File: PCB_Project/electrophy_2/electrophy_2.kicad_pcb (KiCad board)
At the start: 4 copper layers, 35 x 35 mm, 46 parts, among them IC1 ESP32-C3FN4, J1 USB_C_Receptacle_USB2.0_14P, J3 Conn_01x04, SW2 SW_Push, U1 LSM6DSV320XTR, U2 BQ21040DBV, U3 TPS27081ADDCR, U4 USBLC6-2SC6, U5 MIC5504-3.3YM5, Y1 40MHZ 15pf, Y2 32 KHz

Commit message: PCB draft
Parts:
- removed G***: LOGO, ESP32 IMU:Electrophy logo
- J3: footprint Connector_FFC-FPC:Amphenol_F32R-1A7x1-11004_1x04-1MP_P0.5mm_Horizontal -> pogo_pads_4:pogo_pads_4; moved to B.Cu
- moved R10 79.2 mm to (159.5, 112.0), turned to 90 degrees
- moved CH 76.2 mm to (161.2, 111.2), turned to 45 degrees
- moved R11 75.0 mm to (156.4, 110.2)
- moved R12 66.8 mm to (150.6, 103.2)
- moved R13 64.0 mm to (148.3, 103.2)
- moved R14 54.5 mm to (137.3, 104.2), turned to 45 degrees
- moved R15 51.7 mm to (136.4, 103.4), turned to -135 degrees
- moved R9 50.7 mm to (153.6, 113.1), turned to -90 degrees
- moved C1 34.1 mm to (147.8, 112.9), turned to -135 degrees
- moved C10 33.1 mm to (152.8, 101.4), turned to -90 degrees
- moved C12 26.3 mm to (141.1, 101.4)
- moved J3 23.0 mm to (159.6, 90.5), turned to 135 degrees
- moved R3 18.9 mm to (153.1, 110.1), turned to 90 degrees
- moved C3 18.6 mm to (146.2, 112.8), turned to -135 degrees
- moved C2 14.8 mm to (151.4, 107.0), turned to 90 degrees
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- renumbered STA2 to CH, SW2 to ON, STA1 to S1
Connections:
- BAT1 pad 1: BAT_V -> Net-(BAT1-Pin_1)
- C2 pad 1: Net-(U5-VIN) -> BAT_V
- J3 pad 3: SDA -> SCL
- J3 pad 4: SCL -> SDA
- ON pad 1: BAT_V -> Net-(BAT1-Pin_1)
- R11 pad 1: BAT_V -> Net-(BAT1-Pin_1)
- R13 pad 1: BAT_V -> Net-(BAT1-Pin_1)
- R3 pad 1: Net-(U5-VIN) -> BAT_V
- U2 pad 2: BAT_V -> Net-(BAT1-Pin_1)
- U3 pad 2: Net-(U5-VIN) -> BAT_V
- U3 pad 3: Net-(U5-VIN) -> BAT_V
- U3 pad 4: BAT_V -> Net-(BAT1-Pin_1)
- U5 pad 1: Net-(U5-VIN) -> BAT_V
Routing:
- net GND: track 23.5 -> 83.1 mm, vias 32 -> 41
- net POWER_HOLD: track 0.00 -> 42.4 mm, vias 0 -> 2
- net SCL: track 0.75 -> 39.1 mm, vias 0 -> 3
- net Net-(BAT1-Pin_1): track 0.00 -> 38.0 mm, vias 0 -> 2
- net +3.3V: track 3.07 -> 34.3 mm, vias 1 -> 10
- net SDA: track 0.00 -> 27.9 mm, vias 0 -> 1
- net CS: track 0.00 -> 27.6 mm, vias 0 -> 2
- net VBUS: track 6.68 -> 32.2 mm
- net BAT_V: track 0.00 -> 25.2 mm, vias 0 -> 2
- net SCLK: track 0.00 -> 22.6 mm, vias 0 -> 2
- net MOSI: track 0.00 -> 16.5 mm, vias 0 -> 2
- net BAT_MON: track 0.51 -> 16.3 mm
- net MISO: track 0.00 -> 15.5 mm, vias 0 -> 2
- net INT1: track 0.00 -> 14.5 mm, vias 0 -> 2
- net Net-(IC1-GPIO8): track 0.00 -> 8.82 mm, vias 0 -> 2
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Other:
- rule solder_mask_min_width: 0.125 -> 0.1524
- board text added: "3.3v"
- board text added: "ELECTROPHY 2.0"
- board text added: "GND"
- board text added: "SCL"
- board text added: "SDA"
- board text added: "V1"
- board text removed: "BATTERY"
- board text removed: "PWR"
- board text removed: "S"
- board text removed: "V2"

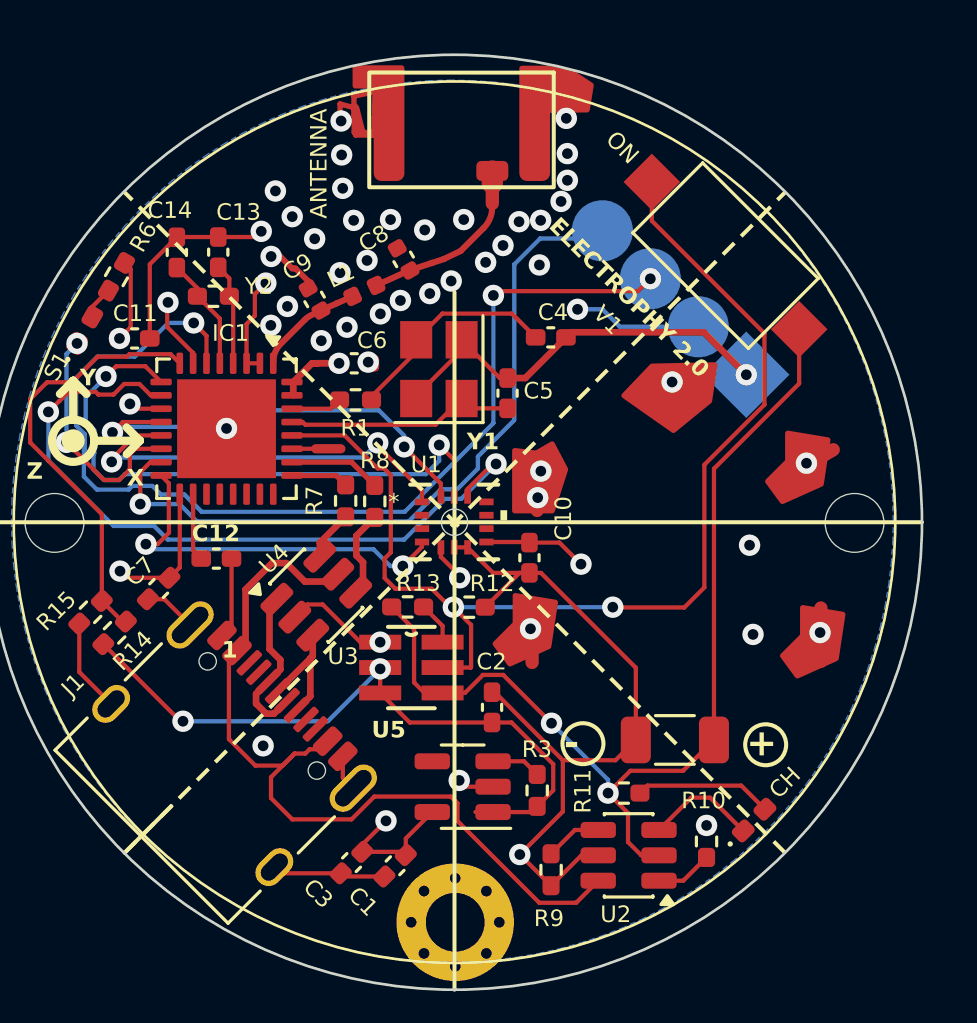
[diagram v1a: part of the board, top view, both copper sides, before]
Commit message: added CC1 and CC2 resistors
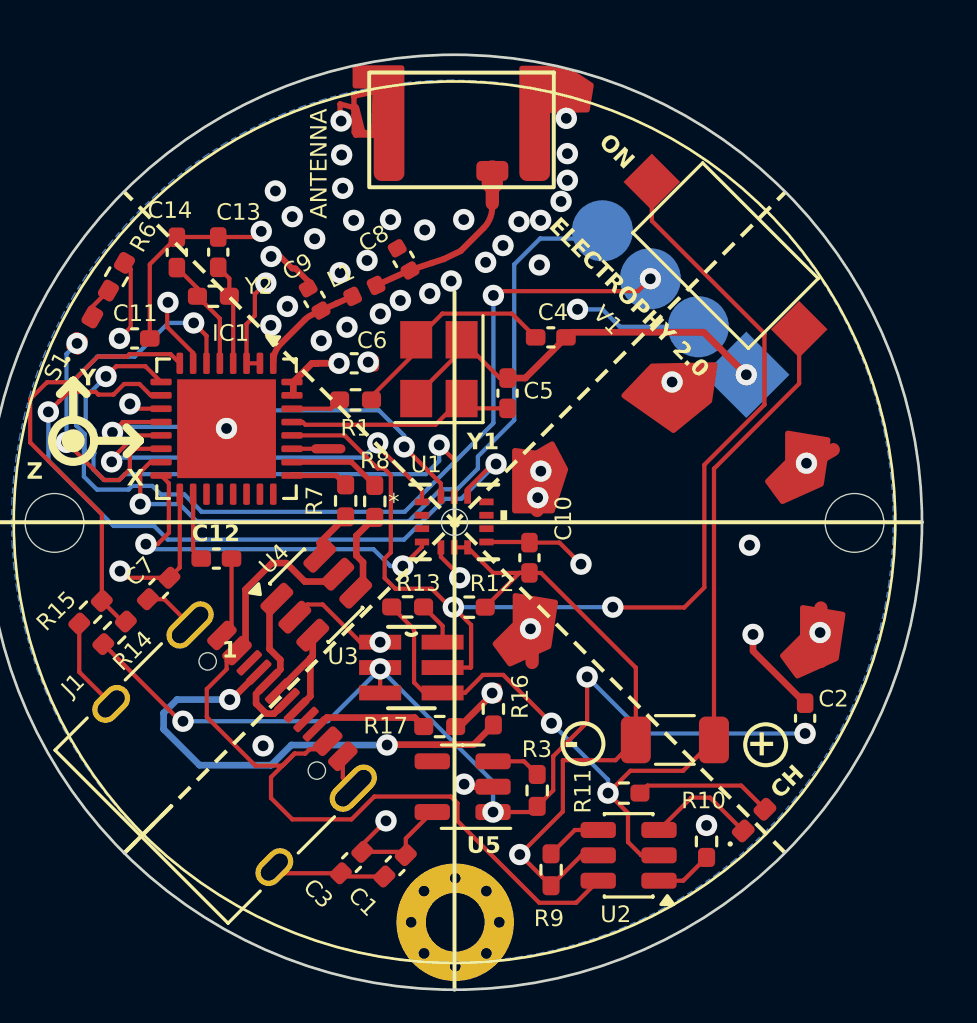
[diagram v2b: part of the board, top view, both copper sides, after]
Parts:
- added R16: 5.1k, Resistor_SMD:R_0402_1005Metric_Pad0.72x0.64mm_HandSolder, F.Cu at (151.5, 107.0)
- added R17: 5.1k, Resistor_SMD:R_0402_1005Metric_Pad0.72x0.64mm_HandSolder, F.Cu at (149.5, 107.7)
- moved C2 11.7 mm to (163.2, 107.4)
- renumbered CH to CH1, ON to ON1
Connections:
- J1 pad A5: unconnected-(J1-CC1-PadA5) -> Net-(J1-CC1)
- J1 pad B5: unconnected-(J1-CC2-PadB5) -> Net-(J1-CC2)
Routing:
- net Net-(J1-CC1): track 0.00 -> 18.3 mm, vias 0 -> 2
- net BAT_V: track 25.2 -> 36.9 mm, vias 2 -> 5
- net Net-(J1-CC2): track 0.00 -> 4.37 mm
- net GND: track 83.1 -> 84.5 mm, vias 41 -> 42
- net VBUS: track 32.2 -> 32.9 mm
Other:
- board text added: "CH"
- board text added: "ON"

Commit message: order placed for ElectroPhy 2.0 V1 PCB
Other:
- rule pad_to_mask_clearance: 0.08 -> 0
- board text removed: "Notes: OLED display pin pads under the PCB"
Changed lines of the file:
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@@
 			(dielectric_constraints yes)
 		)
-		(pad_to_mask_clearance 0.08)
-		(solder_mask_min_width 0.1524)
+		(pad_to_mask_clearance 0)
 		(allow_soldermask_bridges_in_footprints no)
 		(tenting
@@
 		(tags "resistor handsolder")
 		(property "Reference" "R6"
-			(at 1.795378 0.129686 60)
+			(at 0.441077 1.003968 60)
 			(layer "F.SilkS")
 			(effects
@@
 		(tags "capacitor handsolder")
 		(property "Reference" "C12"
-			(at -0.02 -0.94 0)
+			(at -0.09 -0.79 0)
 			(layer "F.SilkS")
 			(effects
@@
 		(tags "resistor handsolder")
 		(property "Reference" "R7"
-			(at 0 -1.17 90)
+			(at -0.21 -1.06 180)
 			(layer "F.SilkS")
 			(effects
@@
 		(tags "capacitor handsolder")
 		(property "Reference" "C10"
-			(at -1.47 -1.27 90)
+			(at 0.01 -0.93 90)
 			(layer "F.SilkS")
 			(effects
@@
 		(tags "capacitor handsolder")
 		(property "Reference" "C11"
-			(at 0.02 -0.94 0)
+			(at 0.57 -0.91 0)
 			(layer "F.SilkS")
 			(effects
@@
 		(tags "capacitor handsolder")
 		(property "Reference" "C14"
-			(at 1.58 -0.26 180)
+			(at 1.41 0.03 180)
 			(layer "F.SilkS")
 			(effects
@@
 		(tags "TPS27081ADDCR ")
 		(property "Reference" "U3"
-			(at -2.56 -0.42 0)
+			(at 2.77 -0.92 0)
 			(unlocked yes)
 			(layer "F.SilkS")
@@
 		(tags "QFN NoLead")
 		(property "Reference" "IC1"
-			(at -3.58 -0.15 0)
+			(at -3.62 -0.63 0)
 			(layer "F.SilkS")
 			(effects
@@
 		(tags "capacitor handsolder")
 		(property "Reference" "C6"
-			(at 0.67 -0.86 0)
+			(at 0.33 -0.83 0)
 			(layer "F.SilkS")
 			(effects
@@
 			(net "unconnected-(U1-SDX-Pad2)")
 			(pinfunction "SDX_2")
-			(pintype "unspecified")
+			(pintype "unspecified+no_connect")
 		)
 		(pad "3" smd rect
@@
 			(net "unconnected-(U1-SCX-Pad3)")
 			(pinfunction "SCX_3")
-			(pintype "unspecified")
+			(pintype "unspecified+no_connect")
 		)
 		(pad "4" smd rect
@@
 			(net "unconnected-(U1-INT2-Pad9)")
 			(pinfunction "INT2_9")
-			(pintype "unspecified")
+			(pintype "unspecified+no_connect")
 		)
 		(pad "10" smd rect
@@
 			(net "unconnected-(U1-OCS_AUX-Pad10)")
 			(pinfunction "OCS_AUX_10")
-			(pintype "unspecified")
+			(pintype "unspecified+no_connect")
 		)
 		(pad "11" smd rect
@@
 			(net "unconnected-(U1-SDO_AUX-Pad11)")
 			(pinfunction "SDO_AUX_11")
-			(pintype "unspecified")
+			(pintype "unspecified+no_connect")
 		)
 		(pad "12" smd rect
@@
 		(tags "LED handsolder")
 		(property "Reference" "S1"
-			(at -1.684134 -0.217006 60)
+			(at -1.671455 -0.155045 60)
 			(layer "F.SilkS")
 			(effects
@@
 		)
 	)
-	(gr_text "Notes:\nOLED display pin pads under the PCB"
-		(at 183.82 73.64 0)
-		(layer "Cmts.User")
-		(effects
-			(font
-				(size 0.62 0.62)
-				(thickness 0.15)
-				(bold yes)
-			)
-			(justify left bottom)
-		)
-	)
 	(dimension
 		(type aligned)
@@
 	)
 	(segment
+		(start 136.46625 91.98245)
+		(end 137.07125 91.37745)
+		(width 0.16)
+		(layer "F.Cu")
+		(net "Net-(S1-A)")
+	)
+	(segment
+		(start 136.46625 92.3642)
+		(end 136.46625 91.98245)
+		(width 0.16)
+		(layer "F.Cu")
+		(net "Net-(S1-A)")
+	)
+	(segment
 		(start 152.83 100.8125)
 		(end 153.9525 100.8125)
@@
 	)
 	(segment
+		(start 147.5 108.39)
+		(end 147.83 108.39)
+		(width 0.25)
+		(layer "F.Cu")
+		(net "Net-(J1-CC1)")
+	)
+	(segment
+		(start 141.67283 106.69)
+		(end 142.696636 105.666194)
+		(width 0.25)
+		(layer "F.Cu")
+		(net "Net-(J1-CC1)")
+	)
+	(segment
+		(start 147.83 108.39)
+		(end 147.845 108.375)
+		(width 0.25)
+		(layer "F.Cu")
+		(net "Net-(J1-CC1)")
+	)
+	(segment
+		(start 141.61 106.69)
+		(end 141.67283 106.69)
+		(width 0.25)
+		(layer "F.Cu")
+		(net "Net-(J1-CC1)")
+	)
+	(segment
+		(start 150.7425 108.375)
+		(end 151.48 107.6375)
+		(width 0.25)
+		(layer "F.Cu")
+		(net "Net-(J1-CC1)")
+	)
+	(segment
+		(start 147.845 108.375)
+		(end 150.7425 108.375)
+		(width 0.25)
+		(layer "F.Cu")
+		(net "Net-(J1-CC1)")
+	)
+	(via
+		(at 141.61 106.69)
+		(size 0.8)
+		(drill 0.4)
+		(layers "F.Cu" "B.Cu")
+		(net "Net-(J1-CC1)")
+	)
+	(via
+		(at 147.5 108.39)
+		(size 0.8)
+		(drill 0.4)
+		(layers "F.Cu" "B.Cu")
+		(net "Net-(J1-CC1)")
+	)
+	(segment
+		(start 143.160305 109.145)
+		(end 140.479695 109.145)
+		(width 0.25)
+		(layer "B.Cu")
+		(net "Net-(J1-CC1)")
+	)
+	(segment
+		(start 140.479695 109.145)
+		(end 139.135 107.800305)
+		(width 0.25)
+		(layer "B.Cu")
+		(net "Net-(J1-CC1)")
+	)
+	(segment
+		(start 139.135 107.192139)
+		(end 139.637139 106.69)
+		(width 0.25)
+		(layer "B.Cu")
+		(net "Net-(J1-CC1)")
+	)
+	(segment
+		(start 139.135 107.800305)
+		(end 139.135 107.192139)
+		(width 0.25)
+		(layer "B.Cu")
+		(net "Net-(J1-CC1)")
+	)
+	(segment
+		(start 147.5 108.39)
+		(end 143.915305 108.39)
+		(width 0.25)
+		(layer "B.Cu")
+		(net "Net-(J1-CC1)")
+	)
+	(segment
+		(start 139.637139 106.69)
+		(end 141.61 106.69)
+		(width 0.25)
+		(layer "B.Cu")
+		(net "Net-(J1-CC1)")
+	)
+	(segment
+		(start 143.915305 108.39)
+		(end 143.160305 109.145)
+		(width 0.25)
+		(layer "B.Cu")
+		(net "Net-(J1-CC1)")
+	)
+	(segment
 		(start 144.628521 105.148521)
 		(end 144.628521 106.562736)
@@
 	)
 	(segment
+		(start 145.242863 107.362608)
+		(end 144.817957 107.787514)
+		(width 0.25)
+		(layer "F.Cu")
+		(net "Net-(J1-CC2)")
+	)
+	(segment
+		(start 148.535108 107.362608)
+		(end 145.242863 107.362608)
+		(width 0.25)
+		(layer "F.Cu")
+		(net "Net-(J1-CC2)")
+	)
+	(segment
+		(start 148.8725 107.7)
+		(end 148.535108 107.362608)
+		(width 0.25)
+		(layer "F.Cu")
+		(net "Net-(J1-CC2)")
+	)
+	(segment
 		(start 144.439999 96.4)
 		(end 149.31 96.4)
@@
 	(segment
 		(start 144.83 97.3)
-		(end 145.77 97.3)
+		(end 145.7 97.3)
 		(width 0.35)
 		(layer "F.Cu")
@@
 	)
 	(segment
-		(start 158.5875 113.47)
-		(end 157.68 113.47)
-		(width 0.16)
-		(layer "F.Cu")
-		(net "Net-(U2-TS)")
-	)
-	(segment
-		(start 159.46 112.5975)
-		(end 158.5875 113.47)
-		(width 0.16)
-		(layer "F.Cu")
-		(net "Net-(U2-TS)")
-	)
-	(segment
 		(start 157.68 111.57)
 		(end 158.89 110.36)
@@
 	)
 	(segment
-		(start 136.46625 91.98245)
-		(end 137.07125 91.37745)
+		(start 158.5875 113.47)
+		(end 157.68 113.47)
 		(width 0.16)
 		(layer "F.Cu")
-		(net "Net-(S1-A)")
+		(net "Net-(U2-TS)")
 	)
 	(segment
-		(start 136.46625 92.3642)
-		(end 136.46625 91.98245)
+		(start 159.46 112.5975)
+		(end 158.5875 113.47)
 		(width 0.16)
 		(layer "F.Cu")
-		(net "Net-(S1-A)")
-	)
-	(segment
-		(start 145.242863 107.362608)
-		(end 144.817957 107.787514)
-		(width 0.25)
-		(layer "F.Cu")
-		(net "Net-(J1-CC2)")
-	)
-	(segment
-		(start 148.535108 107.362608)
-		(end 145.242863 107.362608)
-		(width 0.25)
-		(layer "F.Cu")
-		(net "Net-(J1-CC2)")
-	)
-	(segment
-		(start 148.8725 107.7)
-		(end 148.535108 107.362608)
-		(width 0.25)
-		(layer "F.Cu")
-		(net "Net-(J1-CC2)")
-	)
-	(segment
-		(start 147.5 108.39)
-		(end 147.83 108.39)
-		(width 0.25)
-		(layer "F.Cu")
-		(net "Net-(J1-CC1)")
-	)
-	(segment
-		(start 141.67283 106.69)
-		(end 142.696636 105.666194)
-		(width 0.25)
-		(layer "F.Cu")
-		(net "Net-(J1-CC1)")
-	)
-	(segment
-		(start 147.83 108.39)
-		(end 147.845 108.375)
-		(width 0.25)
-		(layer "F.Cu")
-		(net "Net-(J1-CC1)")
-	)
-	(segment
-		(start 141.61 106.69)
-		(end 141.67283 106.69)
-		(width 0.25)
-		(layer "F.Cu")
-		(net "Net-(J1-CC1)")
-	)
-	(segment
-		(start 150.7425 108.375)
-		(end 151.48 107.6375)
-		(width 0.25)
-		(layer "F.Cu")
-		(net "Net-(J1-CC1)")
-	)
-	(segment
-		(start 147.845 108.375)
-		(end 150.7425 108.375)
-		(width 0.25)
-		(layer "F.Cu")
-		(net "Net-(J1-CC1)")
-	)
-	(via
-		(at 141.61 106.69)
-		(size 0.8)
-		(drill 0.4)
-		(layers "F.Cu" "B.Cu")
-		(net "Net-(J1-CC1)")
-	)
-	(via
-		(at 147.5 108.39)
-		(size 0.8)
-		(drill 0.4)
-		(layers "F.Cu" "B.Cu")
-		(net "Net-(J1-CC1)")
-	)
-	(segment
-		(start 143.160305 109.145)
-		(end 140.479695 109.145)
-		(width 0.25)
-		(layer "B.Cu")
-		(net "Net-(J1-CC1)")
-	)
-	(segment
-		(start 140.479695 109.145)
-		(end 139.135 107.800305)
-		(width 0.25)
-		(layer "B.Cu")
-		(net "Net-(J1-CC1)")
-	)
-	(segment
-		(start 139.135 107.192139)
-		(end 139.637139 106.69)
-		(width 0.25)
-		(layer "B.Cu")
-		(net "Net-(J1-CC1)")
-	)
-	(segment
-		(start 139.135 107.800305)
-		(end 139.135 107.192139)
-		(width 0.25)
-		(layer "B.Cu")
-		(net "Net-(J1-CC1)")
-	)
-	(segment
-		(start 147.5 108.39)
-		(end 143.915305 108.39)
-		(width 0.25)
-		(layer "B.Cu")
-		(net "Net-(J1-CC1)")
-	)
-	(segment
-		(start 139.637139 106.69)
-		(end 141.61 106.69)
-		(width 0.25)
-		(layer "B.Cu")
-		(net "Net-(J1-CC1)")
-	)
-	(segment
-		(start 143.915305 108.39)
-		(end 143.160305 109.145)
-		(width 0.25)
-		(layer "B.Cu")
-		(net "Net-(J1-CC1)")
+		(net "Net-(U2-TS)")
 	)
 	(zone
